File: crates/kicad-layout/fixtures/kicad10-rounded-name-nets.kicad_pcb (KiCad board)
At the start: 2 copper layers, 30 x 20 mm, 2 parts, among them J1 CORPUS_IN, J2 CORPUS_OUT

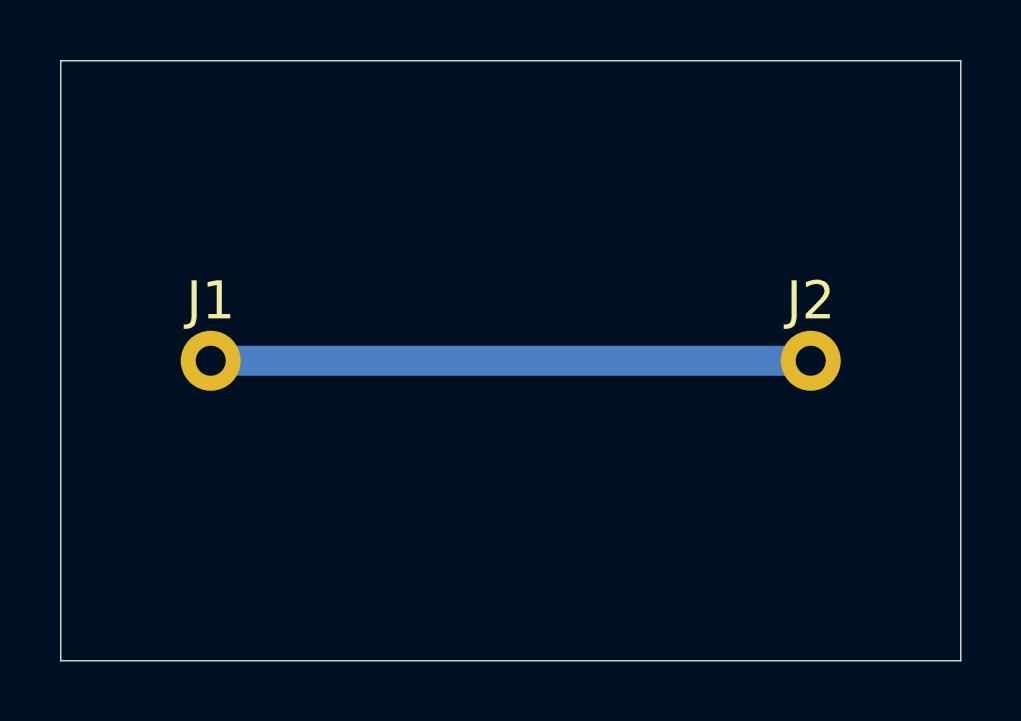
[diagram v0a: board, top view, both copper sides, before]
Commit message: feat: emit validated KiCad route candidates
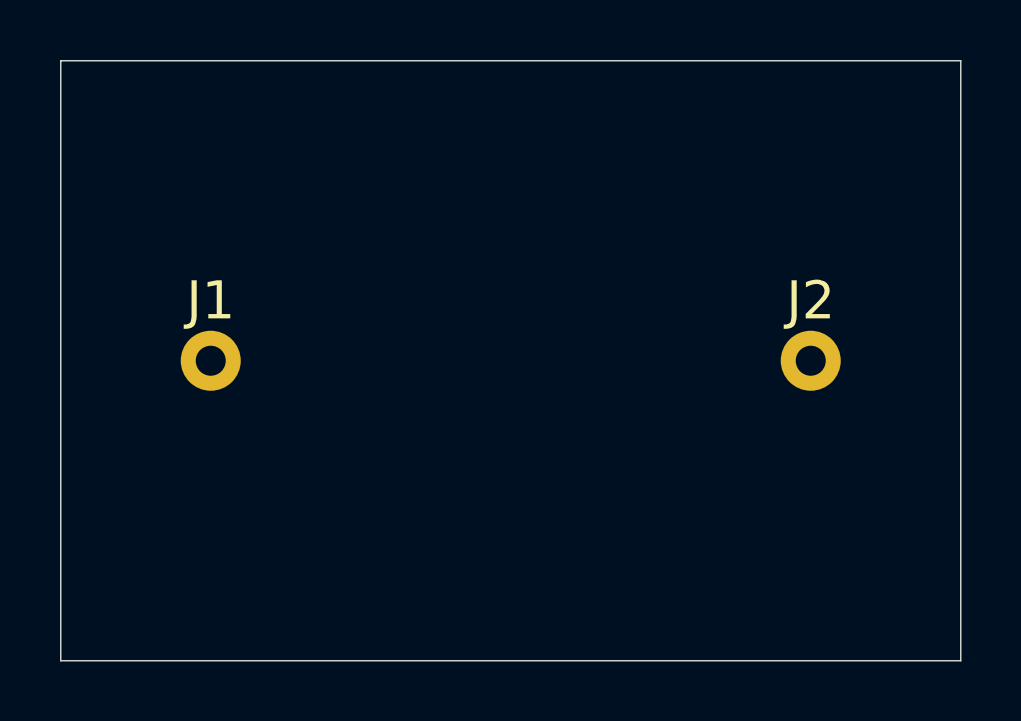
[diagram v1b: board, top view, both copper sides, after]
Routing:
- net SIGNAL: track 20.0 -> 0.00 mm
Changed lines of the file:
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@@
     (layer "Edge.Cuts")
 )
-  (segment
-    (start 5 10)
-    (end 25 10)
-    (width 1)
-    (layer "B.Cu")
-    (net "SIGNAL")
 )
-)
